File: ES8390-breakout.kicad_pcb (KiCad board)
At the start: 4 copper layers, 40.5 x 60 mm, 65 parts, among them CN1 Conn_01x14_Pin, CN2 PJ-327A, CN3 PJ-327A, J1 PJ-603A, J2 Conn_01x02_Pin, J3 Conn_01x02_Pin, U1 TLV9062, U2 LP5907MFX-3.0, U3 ES8390, U4 IM68A130AXTMA1, U5 MAX98306xDT

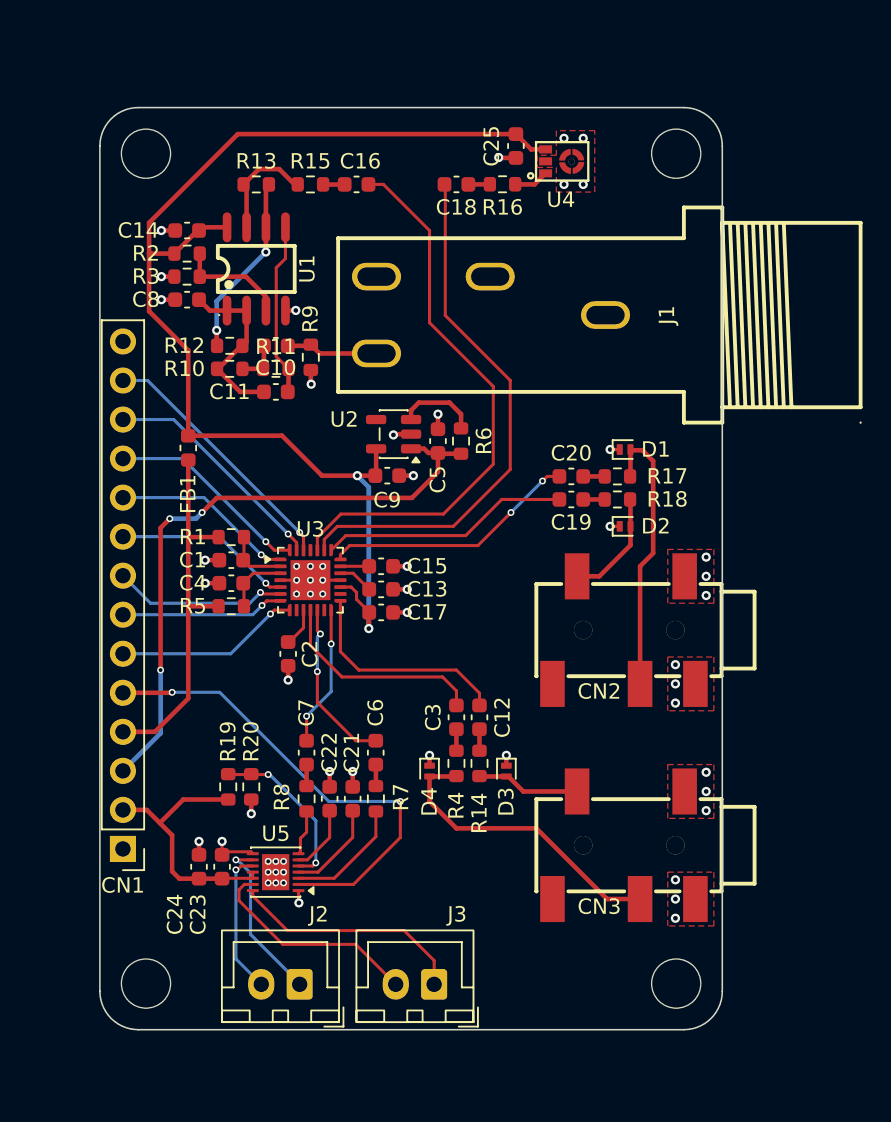
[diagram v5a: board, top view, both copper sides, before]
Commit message: fix lcsc audio footprints
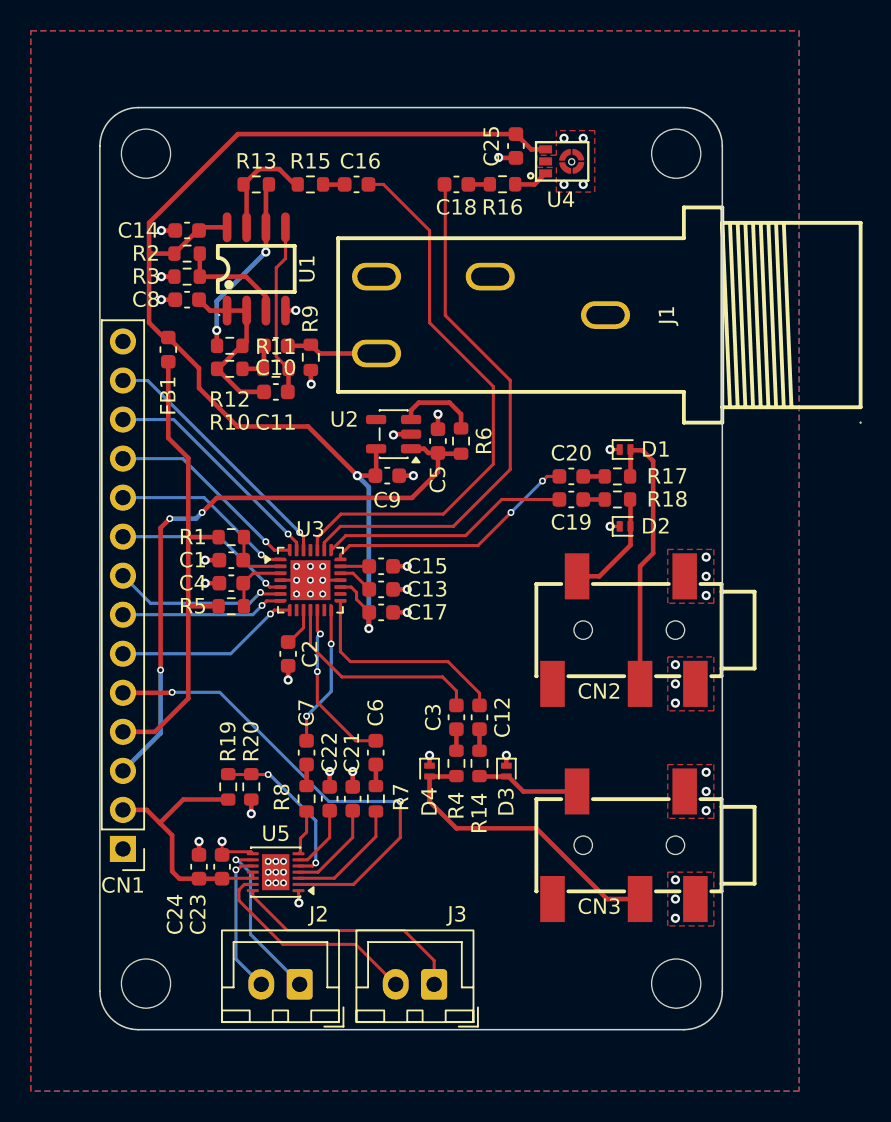
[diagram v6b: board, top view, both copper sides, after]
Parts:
- moved FB1 6.53 mm to (88.0, 73.2)
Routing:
- net VIO: track 24.6 -> 31.5 mm
- net VDDA: track 78.5 -> 76.4 mm
- added copper zone on B.Cu, net GND

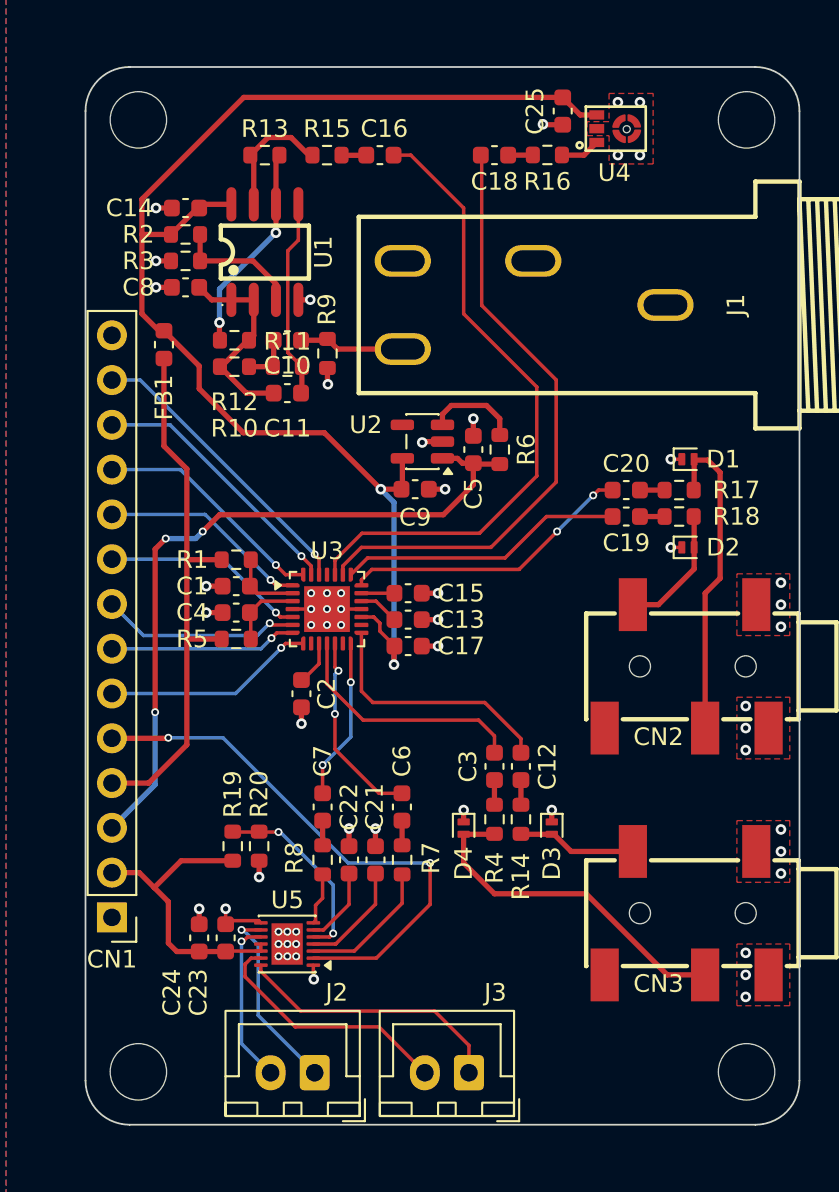
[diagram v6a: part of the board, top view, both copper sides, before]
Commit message: via stitching 5mm
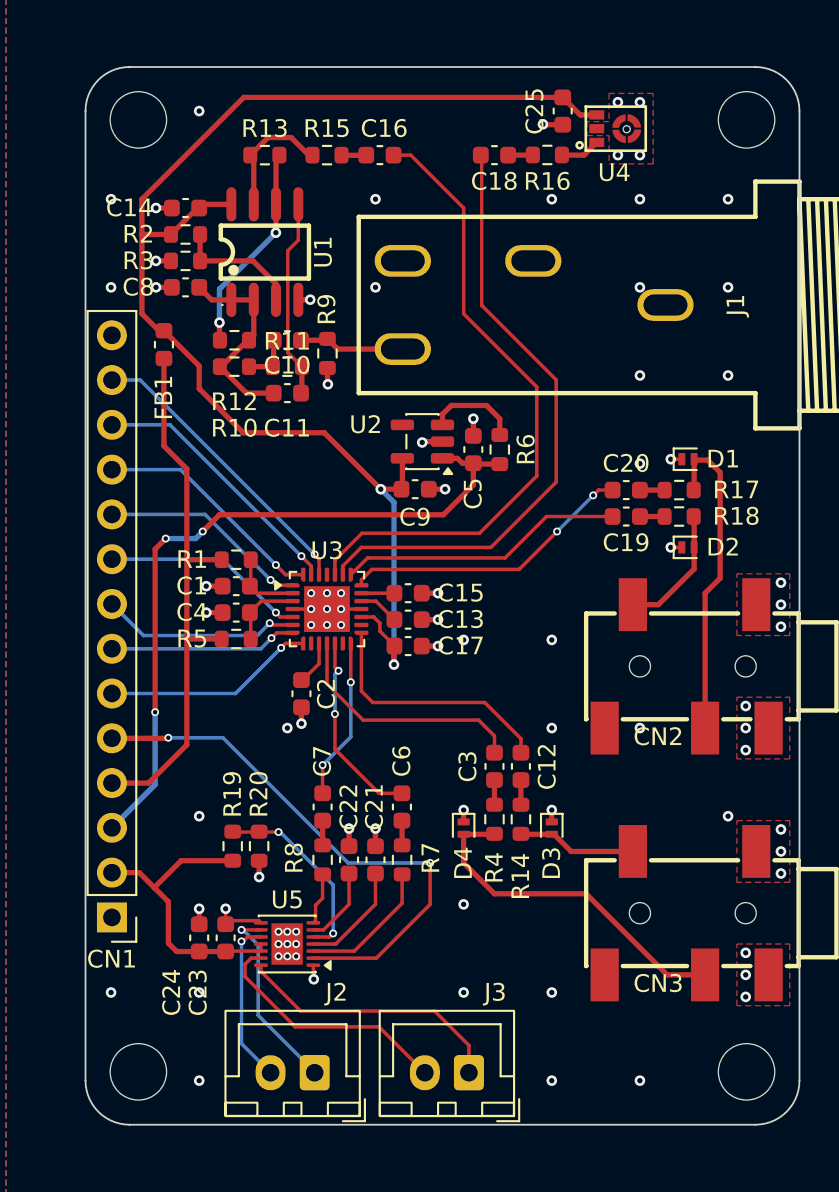
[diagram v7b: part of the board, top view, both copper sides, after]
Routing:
- net GND: vias 59 -> 87
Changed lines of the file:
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@@
+	)
+	(via
+		(at 115 95)
+		(size 0.6)
+		(drill 0.3)
+		(layers "F.Cu" "B.Cu")
+		(free yes)
+		(net "GND")
 	)
 	(via
@@
 	)
 	(via
+		(at 90 60)
+		(size 0.6)
+		(drill 0.3)
+		(layers "F.Cu" "B.Cu")
+		(free yes)
+		(net "GND")
+	)
+	(via
 		(at 91.5 105.25)
 		(size 0.6)
@@
 	)
 	(via
+		(at 110 95)
+		(size 0.6)
+		(drill 0.3)
+		(layers "F.Cu" "B.Cu")
+		(free yes)
+		(net "GND")
+	)
+	(via
 		(at 103.55 88.85)
 		(size 0.6)
@@
 	)
 	(via
+		(at 120 100)
+		(size 0.6)
+		(drill 0.3)
+		(layers "F.Cu" "B.Cu")
+		(free yes)
+		(net "GND")
+	)
+	(via
 		(at 121 93.75)
 		(size 0.6)
@@
 	)
 	(via
+		(at 100 70)
+		(size 0.6)
+		(drill 0.3)
+		(layers "F.Cu" "B.Cu")
+		(free yes)
+		(net "GND")
+	)
+	(via
+		(at 110 110)
+		(size 0.6)
+		(drill 0.3)
+		(layers "F.Cu" "B.Cu")
+		(free yes)
+		(net "GND")
+	)
+	(via
 		(at 95.5 107.95)
 		(size 0.45)
@@
 	)
 	(via
+		(at 90 100)
+		(size 0.6)
+		(drill 0.3)
+		(layers "F.Cu" "B.Cu")
+		(free yes)
+		(net "GND")
+	)
+	(via
 		(at 95.5 107.25)
 		(size 0.45)
@@
 	)
 	(via
+		(at 120 75)
+		(size 0.6)
+		(drill 0.3)
+		(layers "F.Cu" "B.Cu")
+		(free yes)
+		(net "GND")
+	)
+	(via
+		(at 90 110)
+		(size 0.6)
+		(drill 0.3)
+		(layers "F.Cu" "B.Cu")
+		(free yes)
+		(net "GND")
+	)
+	(via
+		(at 115 80)
+		(size 0.6)
+		(drill 0.3)
+		(layers "F.Cu" "B.Cu")
+		(free yes)
+		(net "GND")
+	)
+	(via
+		(at 115 115)
+		(size 0.6)
+		(drill 0.3)
+		(layers "F.Cu" "B.Cu")
+		(free yes)
+		(net "GND")
+	)
+	(via
 		(at 98.05 88.25)
 		(size 0.45)
@@
 	)
 	(via
+		(at 115 75)
+		(size 0.6)
+		(drill 0.3)
+		(layers "F.Cu" "B.Cu")
+		(free yes)
+		(net "GND")
+	)
+	(via
 		(at 113.75 62.5)
 		(size 0.6)
@@
 	)
 	(via
+		(at 90 115)
+		(size 0.6)
+		(drill 0.3)
+		(layers "F.Cu" "B.Cu")
+		(free yes)
+		(net "GND")
+	)
+	(via
+		(at 110 65)
+		(size 0.6)
+		(drill 0.3)
+		(layers "F.Cu" "B.Cu")
+		(free yes)
+		(net "GND")
+	)
+	(via
 		(at 103.95 81.45)
 		(size 0.6)
@@
 	)
 	(via
+		(at 105 90)
+		(size 0.6)
+		(drill 0.3)
+		(layers "F.Cu" "B.Cu")
+		(free yes)
+		(net "GND")
+	)
+	(via
 		(at 90.4 86.95)
 		(size 0.6)
@@
 	)
 	(via
+		(at 85 70)
+		(size 0.6)
+		(drill 0.3)
+		(layers "F.Cu" "B.Cu")
+		(free yes)
+		(net "GND")
+	)
+	(via
+		(at 120 65)
+		(size 0.6)
+		(drill 0.3)
+		(layers "F.Cu" "B.Cu")
+		(free yes)
+		(net "GND")
+	)
+	(via
 		(at 123 86.75)
 		(size 0.6)
@@
 	)
 	(via
+		(at 100 65)
+		(size 0.6)
+		(drill 0.3)
+		(layers "F.Cu" "B.Cu")
+		(free yes)
+		(net "GND")
+	)
+	(via
 		(at 116.75 79.75)
 		(size 0.6)
@@
 	)
 	(via
+		(at 85 110)
+		(size 0.6)
+		(drill 0.3)
+		(layers "F.Cu" "B.Cu")
+		(free yes)
+		(net "GND")
+	)
+	(via
 		(at 95.8 94.75)
 		(size 0.6)
@@
 	)
 	(via
+		(at 95 95)
+		(size 0.6)
+		(drill 0.3)
+		(layers "F.Cu" "B.Cu")
+		(free yes)
+		(net "GND")
+	)
+	(via
 		(at 98.5 100.7)
 		(size 0.6)
@@
 	)
 	(via
+		(at 110 90)
+		(size 0.6)
+		(drill 0.3)
+		(layers "F.Cu" "B.Cu")
+		(free yes)
+		(net "GND")
+	)
+	(via
 		(at 102.65 78.8)
 		(size 0.6)
@@
 	)
 	(via
+		(at 85 65)
+		(size 0.6)
+		(drill 0.3)
+		(layers "F.Cu" "B.Cu")
+		(free yes)
+		(net "GND")
+	)
+	(via
+		(at 105 110)
+		(size 0.6)
+		(drill 0.3)
+		(layers "F.Cu" "B.Cu")
+		(free yes)
+		(net "GND")
+	)
+	(via
 		(at 123 88)
 		(size 0.6)
@@
 	)
 	(via
+		(at 120 70)
+		(size 0.6)
+		(drill 0.3)
+		(layers "F.Cu" "B.Cu")
+		(free yes)
+		(net "GND")
+	)
+	(via
 		(at 87.55 65.5)
 		(size 0.6)
@@
 	)
 	(via
+		(at 110 115)
+		(size 0.6)
+		(drill 0.3)
+		(layers "F.Cu" "B.Cu")
+		(free yes)
+		(net "GND")
+	)
+	(via
 		(at 96.35 87.35)
 		(size 0.45)
@@
 	)
 	(via
+		(at 105 105)
+		(size 0.6)
+		(drill 0.3)
+		(layers "F.Cu" "B.Cu")
+		(free yes)
+		(net "GND")
+	)
+	(via
 		(at 115 62.5)
 		(size 0.6)
@@
 	)
 	(via
+		(at 115 70)
+		(size 0.6)
+		(drill 0.3)
+		(layers "F.Cu" "B.Cu")
+		(free yes)
+		(net "GND")
+	)
+	(via
 		(at 123 100.75)
 		(size 0.6)
 		(drill 0.3)
 		(layers "F.Cu" "B.Cu")
+		(net "GND")
+	)
+	(via
+		(at 115 65)
+		(size 0.6)
+		(drill 0.3)
+		(layers "F.Cu" "B.Cu")
+		(free yes)
 		(net "GND")
 	)
@@
 		)
 		(min_thickness 0.25)
-		(fill
+		(fill yes
 			(thermal_gap 0.5)
 			(thermal_bridge_width 0.5)
@@
 		)
 		(min_thickness 0.25)
-		(fill
+		(fill yes
 			(thermal_gap 0.5)
 			(thermal_bridge_width 0.5)
@@
 		)
 		(min_thickness 0.25)
-		(fill
+		(fill yes
 			(thermal_gap 0.5)
 			(thermal_bridge_width 0.5)
@@
 		)
 		(min_thickness 0.25)
-		(fill
+		(fill yes
 			(thermal_gap 0.5)
 			(thermal_bridge_width 0.5)
@@
 		)
 		(min_thickness 0.25)
-		(fill
+		(fill yes
 			(thermal_gap 0.5)
 			(thermal_bridge_width 0.5)
@@
 		)
 		(min_thickness 0.25)
-		(fill
+		(fill yes
 			(thermal_gap 0.5)
 			(thermal_bridge_width 0.5)

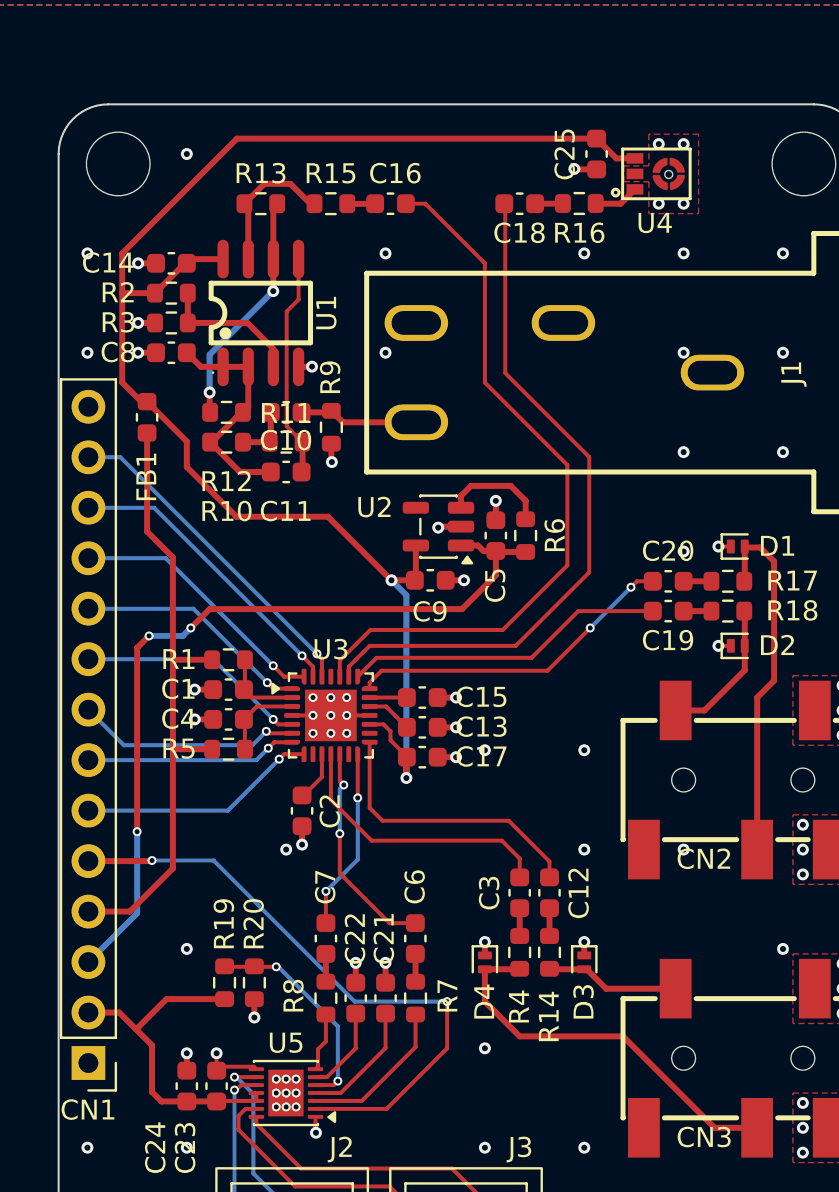
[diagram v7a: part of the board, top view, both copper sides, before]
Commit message: replace microphone with top port MEMS MSM381ACP003
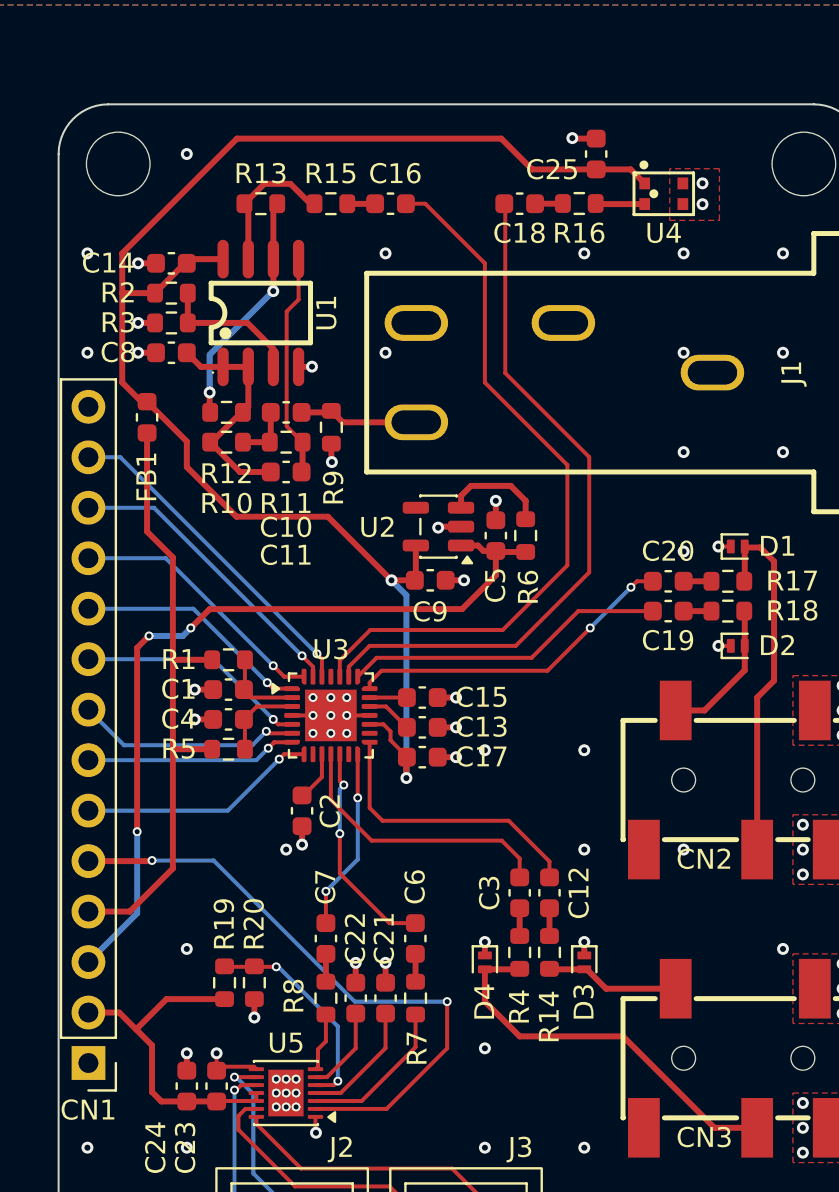
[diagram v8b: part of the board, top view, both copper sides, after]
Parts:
- CN1: value Conn_01x14_Pin -> 1x14_P2.54mm
- J2, J3: value Conn_01x02_Pin -> JST_XH_B2B
- U4: value IM68A130AXTMA1 -> MSM381ACP003_C51928212; footprint lcsc:MIC-SMD_4P-L3.4-W2.5_IM68A130V01 -> lcsc:MIC-SMD_4P-L2.8-W1.9-TR_MSM381ACP003
- moved U4 1.07 mm to (114.0, 62.0)
- turned C25 to 90 degrees
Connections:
- U4 pad 1: RIN1 -> VDDA
- U4 pad 2: GND -> RIN1
- U4 pad 3: VDDA -> GND
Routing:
- net VDDA: track 76.4 -> 77.4 mm
- net GND: vias 87 -> 85
